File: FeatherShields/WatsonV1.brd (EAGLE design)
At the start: 49.5 x 23 mm, 11 parts

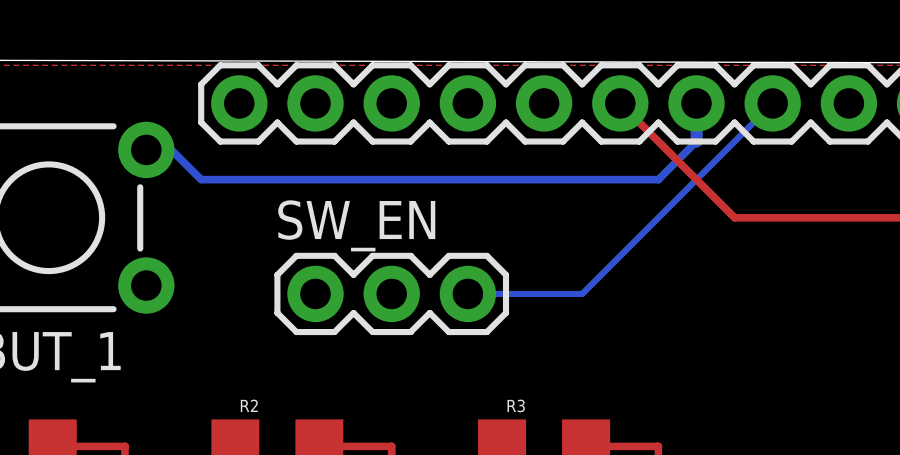
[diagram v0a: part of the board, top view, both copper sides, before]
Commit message: Fixed airwire
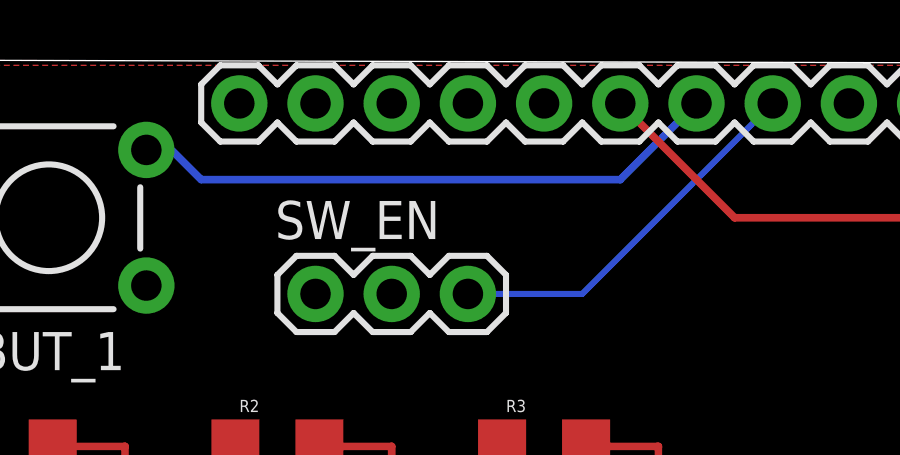
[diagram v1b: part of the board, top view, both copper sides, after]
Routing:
- net BUTT: track 20.8 -> 20.0 mm
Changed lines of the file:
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@@
 <?xml version="1.0" encoding="utf-8"?>
 <!DOCTYPE eagle SYSTEM "eagle.dtd">
-<eagle version="9.3.1">
+<eagle version="9.6.2">
 <drawing>
 <settings>
@@
 <wire x1="9.8806" y1="20.0406" x2="10.16" y2="20.32" width="0.254" layer="16"/>
 <wire x1="10.16" y1="20.32" x2="11.43" y2="19.05" width="0.254" layer="16"/>
-<wire x1="11.43" y1="19.05" x2="26.67" y2="19.05" width="0.254" layer="16"/>
-<wire x1="26.67" y1="19.05" x2="27.94" y2="20.32" width="0.254" layer="16"/>
-<wire x1="27.94" y1="20.32" x2="27.94" y2="21.59" width="0.4064" layer="16"/>
+<wire x1="11.43" y1="19.05" x2="25.4" y2="19.05" width="0.254" layer="16"/>
+<wire x1="25.4" y1="19.05" x2="27.94" y2="21.59" width="0.254" layer="16"/>
 </signal>
 </signals>
